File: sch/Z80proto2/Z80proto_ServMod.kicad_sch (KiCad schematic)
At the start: 21 parts

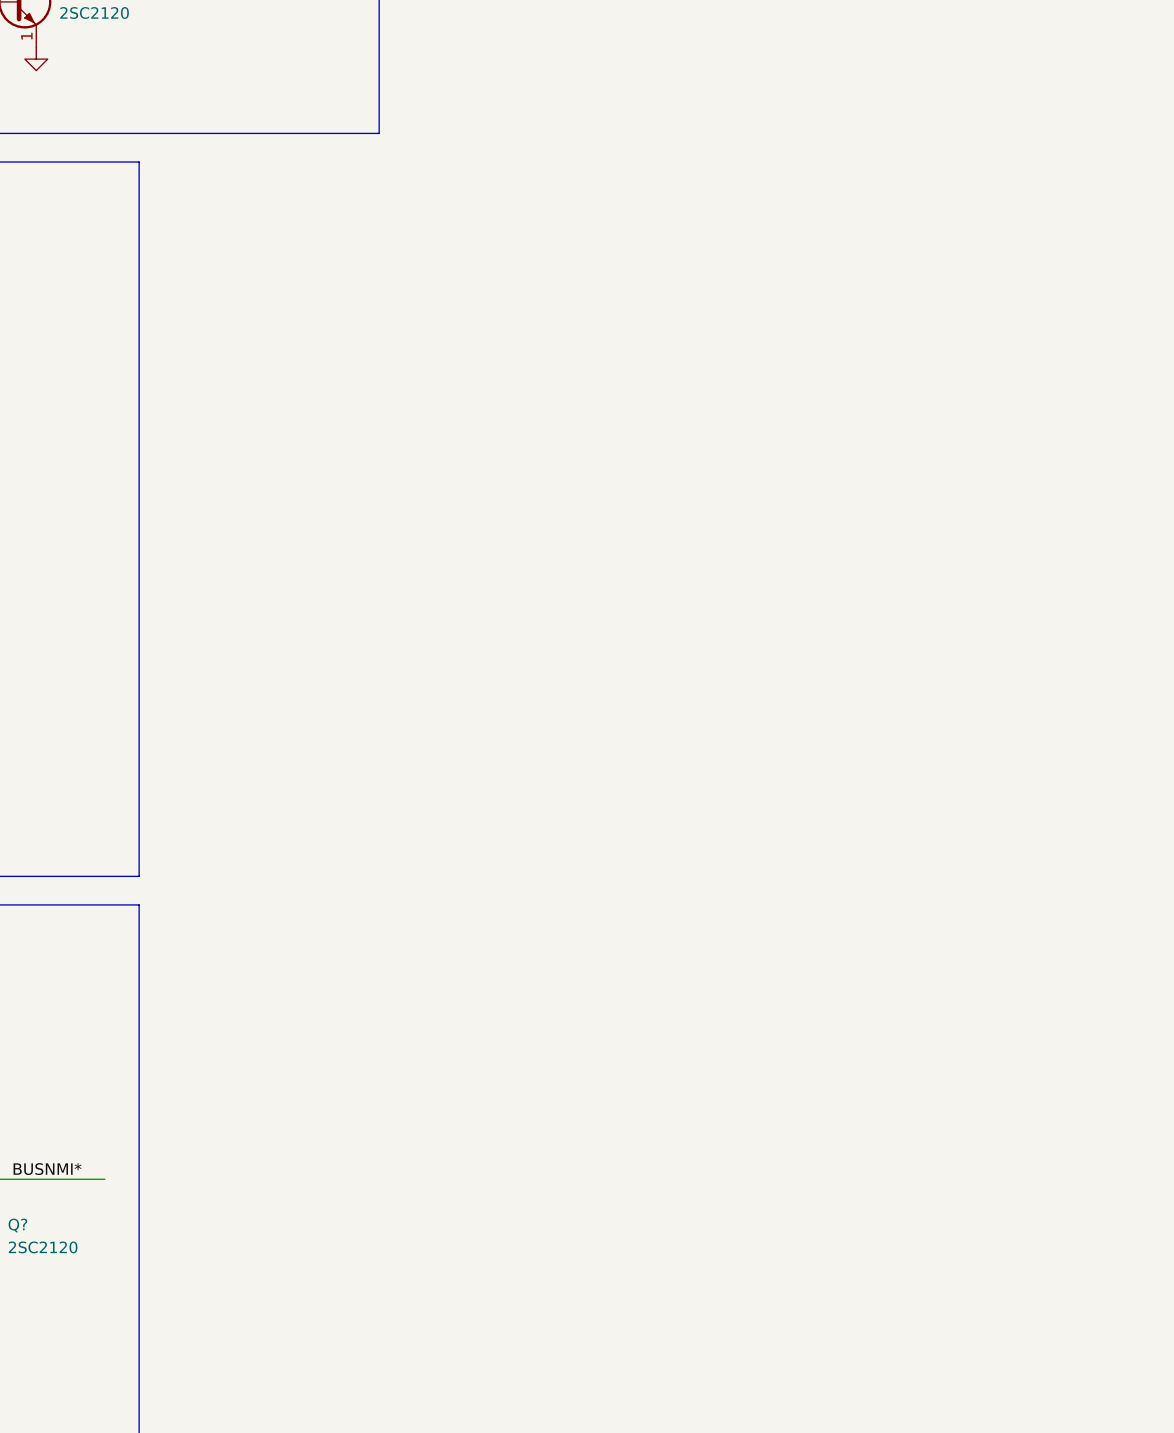
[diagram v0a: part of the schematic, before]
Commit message: Switch zcc to sdcc
Switch compiler
(xymodem.c doesn't work)
Add WAIT cycle circuit(HC191), still testing ...
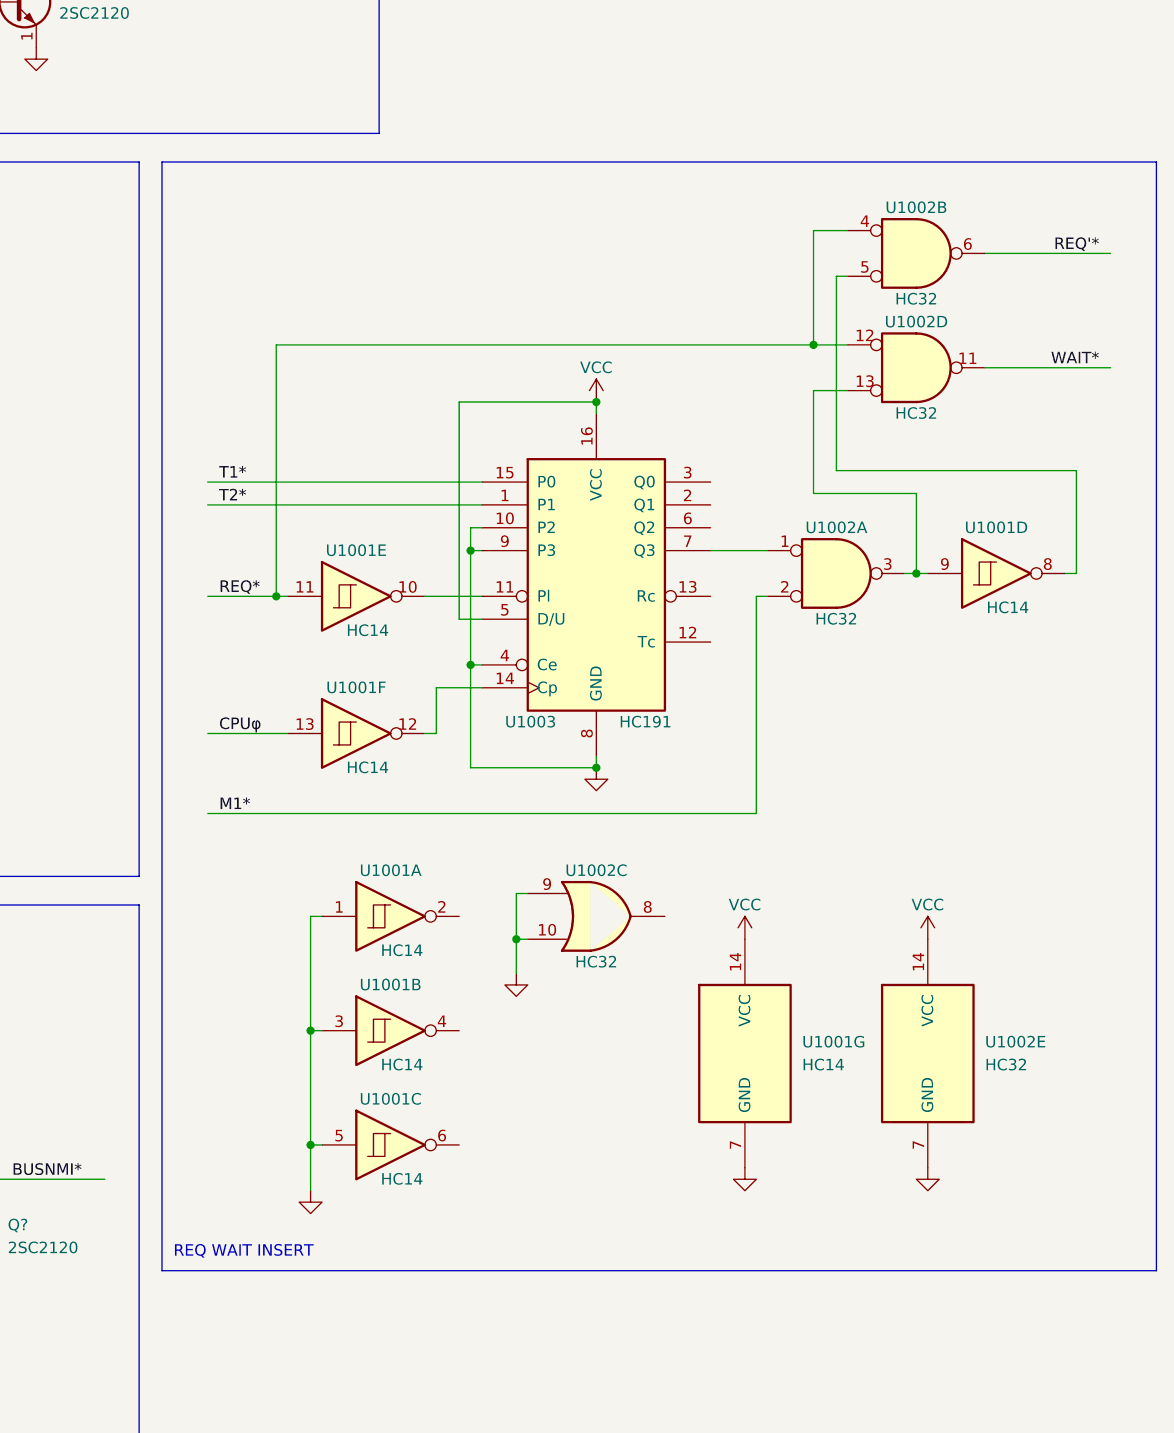
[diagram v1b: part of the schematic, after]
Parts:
- added U1001: HC14, symbol 74xx:74LS14
- added U1002: HC32, symbol 74xx:74LS32
- added U1003: HC191, symbol 74xx:74LS191
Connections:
- net CPUφ: now also U1001.13
- net GND: now also U1001.1, U1001.3, U1001.5, U1001.7 (GND), U1002.10, U1002.7 (GND), U1002.9, U1003.10 (P2), U1003.4 (Ce), U1003.8 (GND), U1003.9 (P3)
- net VCC: now also U1001.14 (VCC), U1002.14 (VCC), U1003.16 (VCC), U1003.5 (D/U)
- new net: U1001.10, U1003.11 (Pl)
- new net: U1001.8, U1002.5
- new net: U1001.9, U1002.13, U1002.3
- new net: U1001.12, U1003.14 (Cp)
- new net: U1002.1, U1003.7 (Q3)
- new net M1*: U1002.2
- new net REQ'*: U1002.6
- new net REQ*: U1001.11, U1002.12, U1002.4
- new net T1*: U1003.15 (P0)
- new net T2*: U1003.1 (P1)
- new net WAIT*: U1002.11
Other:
- note added: "REQ WAIT INSERT"
